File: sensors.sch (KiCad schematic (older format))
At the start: 8 parts, among them U12 LIS2HH12, U8 VL53L0X

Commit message: screen attached!
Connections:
- net RF_SD: no longer names the net of R58.2, U8.5 (XSHUT)
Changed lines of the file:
@@
 $Descr A4 11693 8268
 encoding utf-8
-Sheet 12 15
+Sheet 12 14
 Title ""
 Date ""
@@
 NoConn ~ 5900 3900
 $Comp
-L GND-RESCUE-DFTBoard #PWR0160
+L GND-RESCUE-DFTBoard #PWR0153
 U 1 1 58598433
 P 4550 4150
-F 0 "#PWR0160" H 4550 4150 30  0001 C CNN
+F 0 "#PWR0153" H 4550 4150 30  0001 C CNN
 F 1 "GND" H 4550 4080 30  0001 C CNN
 F 2 "" H 4550 4150 60  0001 C CNN
@@
 	4550 3400 4550 3300
 Connection ~ 4550 3300
-Text GLabel 6400 3300 2    60   Input ~ 0
-RF_SD
 $Comp
 L R R58
@@
 	1    0    0    -1
 $EndComp
-Wire Wire Line
-	5900 3300 6400 3300
-$Comp
-L +1.8V #PWR0161
+$Comp
+L +1.8V #PWR0154
 U 1 1 585987BD
 P 6200 2550
-F 0 "#PWR0161" H 6200 2690 20  0001 C CNN
+F 0 "#PWR0154" H 6200 2690 20  0001 C CNN
 F 1 "+1.8V" H 6200 2660 30  0000 C CNN
 F 2 "" H 6200 2550 60  0001 C CNN
@@
 Wire Wire Line
 	6300 3400 6300 2900
-Connection ~ 6100 3300
 Connection ~ 6300 3400
 Text GLabel 6400 3400 2    60   Input ~ 0
 RF_IRQ
 $Comp
-L +3.3V #PWR0162
+L +3.3V #PWR0155
 U 1 1 587438B2
 P 4000 3200
-F 0 "#PWR0162" H 4000 3050 50  0001 C CNN
+F 0 "#PWR0155" H 4000 3050 50  0001 C CNN
 F 1 "+3.3V" H 4000 3340 50  0000 C CNN
 F 2 "" H 4000 3200 50  0000 C CNN
@@
 $EndComp
 $Comp
-L GND-RESCUE-DFTBoard #PWR0163
+L GND-RESCUE-DFTBoard #PWR0156
 U 1 1 5983B53E
 P 6050 5400
-F 0 "#PWR0163" H 6050 5400 30  0001 C CNN
+F 0 "#PWR0156" H 6050 5400 30  0001 C CNN
 F 1 "GND" H 6050 5330 30  0001 C CNN
 F 2 "" H 6050 5400 60  0001 C CNN
@@
 I2C_SCLK
 $Comp
-L +1.8V #PWR0164
+L +1.8V #PWR0157
 U 1 1 5983B702
 P 4050 4500
-F 0 "#PWR0164" H 4050 4640 20  0001 C CNN
+F 0 "#PWR0157" H 4050 4640 20  0001 C CNN
 F 1 "+1.8V" H 4050 4610 30  0000 C CNN
 F 2 "" H 4050 4500 60  0001 C CNN
@@
 Connection ~ 4050 4750
 $Comp
-L +1.8V #PWR0165
+L +1.8V #PWR0158
 U 1 1 5983B8A0
 P 6150 4500
-F 0 "#PWR0165" H 6150 4640 20  0001 C CNN
+F 0 "#PWR0158" H 6150 4640 20  0001 C CNN
 F 1 "+1.8V" H 6150 4610 30  0000 C CNN
 F 2 "" H 6150 4500 60  0001 C CNN
@@
 	6450 4950 6450 4850
 $Comp
-L GND-RESCUE-DFTBoard #PWR0166
+L GND-RESCUE-DFTBoard #PWR0159
 U 1 1 5983BAD9
 P 6150 4950
-F 0 "#PWR0166" H 6150 4950 30  0001 C CNN
+F 0 "#PWR0159" H 6150 4950 30  0001 C CNN
 F 1 "GND" H 6150 4880 30  0001 C CNN
 F 2 "" H 6150 4950 60  0001 C CNN
@@
 $EndComp
 $Comp
-L GND-RESCUE-DFTBoard #PWR0167
+L GND-RESCUE-DFTBoard #PWR0160
 U 1 1 5983BAFC
 P 6450 4950
-F 0 "#PWR0167" H 6450 4950 30  0001 C CNN
+F 0 "#PWR0160" H 6450 4950 30  0001 C CNN
 F 1 "GND" H 6450 4880 30  0001 C CNN
 F 2 "" H 6450 4950 60  0001 C CNN
@@
 	6150 4500 6150 4650
 $Comp
-L GND-RESCUE-DFTBoard #PWR0168
+L GND-RESCUE-DFTBoard #PWR0161
 U 1 1 5983BD80
 P 4450 5350
-F 0 "#PWR0168" H 4450 5350 30  0001 C CNN
+F 0 "#PWR0161" H 4450 5350 30  0001 C CNN
 F 1 "GND" H 4450 5280 30  0001 C CNN
 F 2 "" H 4450 5350 60  0001 C CNN
@@
 NoConn ~ 4750 5150
 NoConn ~ 4750 5250
+Wire Wire Line
+	6100 3300 5900 3300
 $EndSCHEMATC

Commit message: using BOMs AWAY to create BOM
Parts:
- C110, C97: MFR (none) -> Murata; MPN (none) -> GRM188R71C104KA01D
- C111, C98: MFR (none) -> Murata; MPN (none) -> GRM21BR61A475KA73L
- R58, R59: MFR (none) -> Vishay Dale; MPN (none) -> CRCW040210K0FKED
- U8: MFR (none) -> STMicroelectronics; MPN (none) -> VL53L0CXV0DH/1

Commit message: just added NOTE field to BOMS AWAY
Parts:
- C110, C97: SPN (none) -> 490-1532-1-ND; SPR (none) -> Digikey
- C111, C98: SPN (none) -> 490-9750-1-ND; SPR (none) -> Digikey
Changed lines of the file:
@@
 F 4 "Murata" H 0 0 50 0001 C CNN "MFR"
 F 5 "GRM21BR61A475KA73L" H 0 0 50 0001 C CNN "MPN"
-F 6 "" H 0 0 50 0001 C CNN "SPR"
-F 7 "" H 0 0 50 0001 C CNN "SPN"
+F 6 "Digikey" H 0 0 50 0001 C CNN "SPR"
+F 7 "490-9750-1-ND" H 0 0 50 0001 C CNN "SPN"
 F 8 "" H 0 0 50 0001 C CNN "SPURL"
 	1    4000 3400
@@
 F 4 "Murata" H 0 0 50 0001 C CNN "MFR"
 F 5 "GRM188R71C104KA01D" H 0 0 50 0001 C CNN "MPN"
-F 6 "" H 0 0 50 0001 C CNN "SPR"
-F 7 "" H 0 0 50 0001 C CNN "SPN"
+F 6 "Digikey" H 0 0 50 0001 C CNN "SPR"
+F 7 "490-1532-1-ND" H 0 0 50 0001 C CNN "SPN"
 F 8 "" H 0 0 50 0001 C CNN "SPURL"
 	1    3700 3400
@@
 F 4 "Murata" H 0 0 50 0001 C CNN "MFR"
 F 5 "GRM21BR61A475KA73L" H 0 0 50 0001 C CNN "MPN"
-F 6 "" H 0 0 50 0001 C CNN "SPR"
-F 7 "" H 0 0 50 0001 C CNN "SPN"
+F 6 "Digikey" H 0 0 50 0001 C CNN "SPR"
+F 7 "490-9750-1-ND" H 0 0 50 0001 C CNN "SPN"
 F 8 "" H 0 0 50 0001 C CNN "SPURL"
 	1    6450 4750
@@
 F 4 "Murata" H 0 0 50 0001 C CNN "MFR"
 F 5 "GRM188R71C104KA01D" H 0 0 50 0001 C CNN "MPN"
-F 6 "" H 0 0 50 0001 C CNN "SPR"
-F 7 "" H 0 0 50 0001 C CNN "SPN"
+F 6 "Digikey" H 0 0 50 0001 C CNN "SPR"
+F 7 "490-1532-1-ND" H 0 0 50 0001 C CNN "SPN"
 F 8 "" H 0 0 50 0001 C CNN "SPURL"
 	1    6150 4750

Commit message: Complete BOM. all resistors now 0402
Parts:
- R58, R59: MFR Vishay Dale -> Yageo; MPN CRCW040210K0FKED -> RC0402FR-0710KL; SPN (none) -> 311-10.0KLRTR-ND; SPR (none) -> Digikey
- U12: MFR (none) -> STMicroelectronics; MPN (none) -> LIS2HH12TR; SPN (none) -> 497-15069-1-ND; SPR (none) -> Digikey
- U8: SPN (none) -> 497-16538-1-ND; SPR (none) -> Digikey

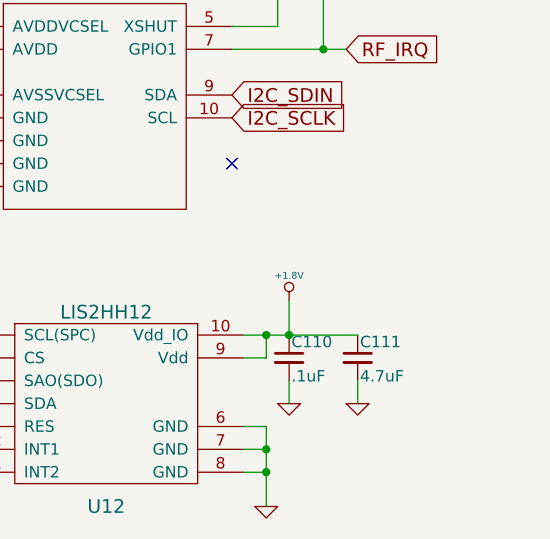
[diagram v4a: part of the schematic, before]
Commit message: added caps to audio
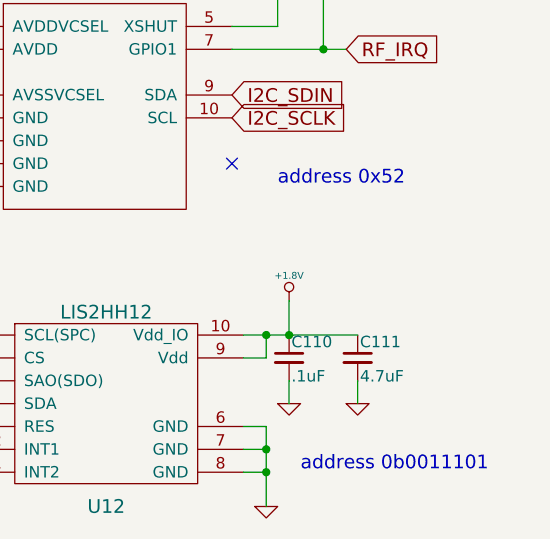
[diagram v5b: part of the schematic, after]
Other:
- note added: "address 0b0011101"
- note added: "address 0x52"
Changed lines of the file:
@@
 $Descr A4 11693 8268
 encoding utf-8
-Sheet 12 14
+Sheet 11 14
 Title ""
 Date ""
@@
 $EndComp
 $Comp
-L GND-RESCUE-DFTBoard #PWR0153
+L GND-RESCUE-DFTBoard #PWR0154
 U 1 1 58598433
 P 4550 4150
-F 0 "#PWR0153" H 4550 4150 30  0001 C CNN
+F 0 "#PWR0154" H 4550 4150 30  0001 C CNN
 F 1 "GND" H 4550 4080 30  0001 C CNN
 F 2 "" H 4550 4150 60  0001 C CNN
@@
 $EndComp
 $Comp
-L +1.8V #PWR0154
+L +1.8V #PWR0155
 U 1 1 585987BD
 P 6200 2550
-F 0 "#PWR0154" H 6200 2690 20  0001 C CNN
+F 0 "#PWR0155" H 6200 2690 20  0001 C CNN
 F 1 "+1.8V" H 6200 2660 30  0000 C CNN
 F 2 "" H 6200 2550 60  0001 C CNN
@@
 $EndComp
 $Comp
-L +3.3V #PWR0155
+L +3.3V #PWR0156
 U 1 1 587438B2
 P 4000 3200
-F 0 "#PWR0155" H 4000 3050 50  0001 C CNN
+F 0 "#PWR0156" H 4000 3050 50  0001 C CNN
 F 1 "+3.3V" H 4000 3340 50  0000 C CNN
 F 2 "" H 4000 3200 50  0000 C CNN
@@
 $EndComp
 $Comp
-L GND-RESCUE-DFTBoard #PWR0156
+L GND-RESCUE-DFTBoard #PWR0157
 U 1 1 5983B53E
 P 6050 5400
-F 0 "#PWR0156" H 6050 5400 30  0001 C CNN
+F 0 "#PWR0157" H 6050 5400 30  0001 C CNN
 F 1 "GND" H 6050 5330 30  0001 C CNN
 F 2 "" H 6050 5400 60  0001 C CNN
@@
 $EndComp
 $Comp
-L +1.8V #PWR0157
+L +1.8V #PWR0158
 U 1 1 5983B702
 P 4050 4500
-F 0 "#PWR0157" H 4050 4640 20  0001 C CNN
+F 0 "#PWR0158" H 4050 4640 20  0001 C CNN
 F 1 "+1.8V" H 4050 4610 30  0000 C CNN
 F 2 "" H 4050 4500 60  0001 C CNN
@@
 $EndComp
 $Comp
-L +1.8V #PWR0158
+L +1.8V #PWR0159
 U 1 1 5983B8A0
 P 6150 4500
-F 0 "#PWR0158" H 6150 4640 20  0001 C CNN
+F 0 "#PWR0159" H 6150 4640 20  0001 C CNN
 F 1 "+1.8V" H 6150 4610 30  0000 C CNN
 F 2 "" H 6150 4500 60  0001 C CNN
@@
 $EndComp
 $Comp
-L GND-RESCUE-DFTBoard #PWR0159
+L GND-RESCUE-DFTBoard #PWR0160
 U 1 1 5983BAD9
 P 6150 4950
-F 0 "#PWR0159" H 6150 4950 30  0001 C CNN
+F 0 "#PWR0160" H 6150 4950 30  0001 C CNN
 F 1 "GND" H 6150 4880 30  0001 C CNN
 F 2 "" H 6150 4950 60  0001 C CNN
@@
 $EndComp
 $Comp
-L GND-RESCUE-DFTBoard #PWR0160
+L GND-RESCUE-DFTBoard #PWR0161
 U 1 1 5983BAFC
 P 6450 4950
-F 0 "#PWR0160" H 6450 4950 30  0001 C CNN
+F 0 "#PWR0161" H 6450 4950 30  0001 C CNN
 F 1 "GND" H 6450 4880 30  0001 C CNN
 F 2 "" H 6450 4950 60  0001 C CNN
@@
 $EndComp
 $Comp
-L GND-RESCUE-DFTBoard #PWR0161
+L GND-RESCUE-DFTBoard #PWR0162
 U 1 1 5983BD80
 P 4450 5350
-F 0 "#PWR0161" H 4450 5350 30  0001 C CNN
+F 0 "#PWR0162" H 4450 5350 30  0001 C CNN
 F 1 "GND" H 4450 5280 30  0001 C CNN
 F 2 "" H 4450 5350 60  0001 C CNN
@@
 NoConn ~ 4750 5150
 NoConn ~ 4750 5250
+Text Notes 6100 4000 0    60   ~ 0
+address 0x52
+Text Notes 6200 5250 0    60   ~ 0
+address 0b0011101
 $EndSCHEMATC

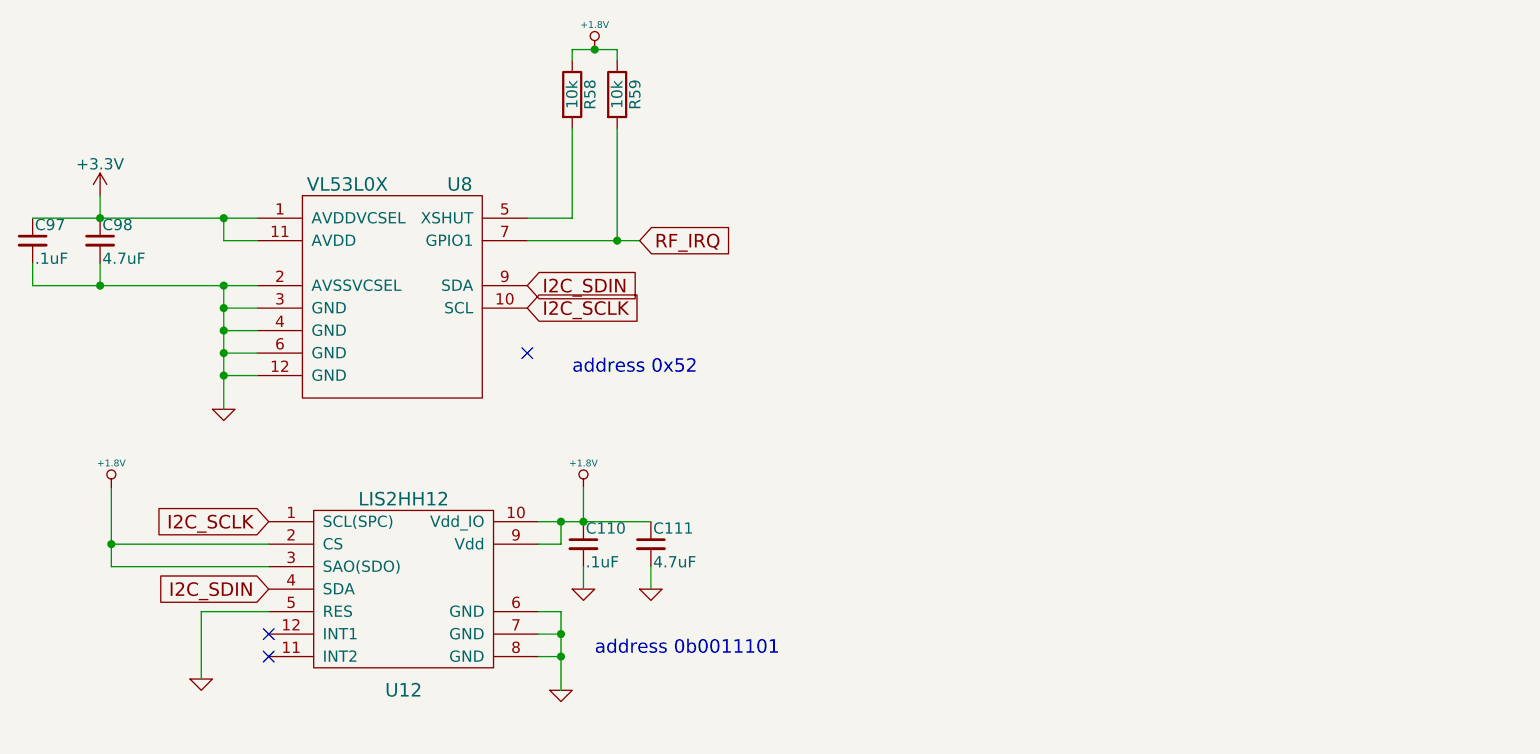
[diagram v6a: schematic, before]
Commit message: about to resize all silkscreen text to 0.5
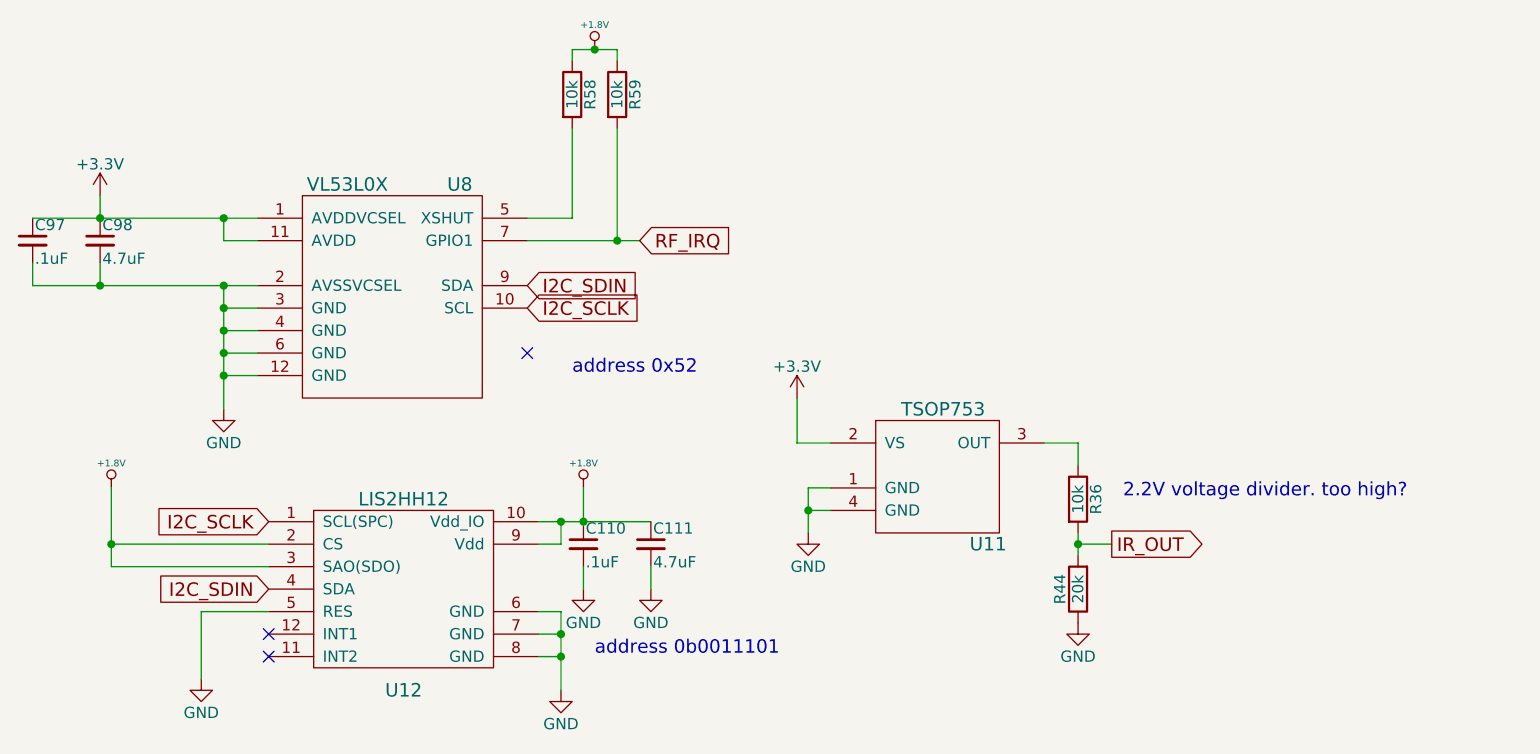
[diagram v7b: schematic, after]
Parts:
- added R36: 10k, Resistors_SMD:R_0402, symbol R
- added R44: 20k, Resistors_SMD:R_0402, symbol R
- added U11: TSOP753, DFTcustom:TSOP753_755, symbol TSOP753
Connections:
- net +3V3: now also U11.2 (VS)
- net GND: now also R44.1, U11.1 (GND), U11.4 (GND)
- new net: R36.1, U11.3 (OUT)
- new net IR_OUT: R36.2, R44.2
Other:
- note added: "2.2V voltage divider. too high?"
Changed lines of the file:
@@
 LIBS:er-con06hb-1
 LIBS:jack_trs_4pins
+LIBS:NorBot
+LIBS:CC2500
 EELAYER 25 0
 EELAYER END
 $Descr A4 11693 8268
 encoding utf-8
-Sheet 11 14
+Sheet 11 15
 Title ""
 Date ""
@@
 $EndComp
 $Comp
-L GND-RESCUE-DFTBoard #PWR0154
-U 1 1 58598433
-P 4550 4150
-F 0 "#PWR0154" H 4550 4150 30  0001 C CNN
-F 1 "GND" H 4550 4080 30  0001 C CNN
-F 2 "" H 4550 4150 60  0001 C CNN
-F 3 "" H 4550 4150 60  0001 C CNN
-	1    4550 4150
-	1    0    0    -1
-$EndComp
-$Comp
 L C_Small C98
 U 1 1 585984E0
@@
 $EndComp
 $Comp
-L +1.8V #PWR0155
+L +1.8V #PWR0149
 U 1 1 585987BD
 P 6200 2550
-F 0 "#PWR0155" H 6200 2690 20  0001 C CNN
+F 0 "#PWR0149" H 6200 2690 20  0001 C CNN
 F 1 "+1.8V" H 6200 2660 30  0000 C CNN
 F 2 "" H 6200 2550 60  0001 C CNN
@@
 $EndComp
 $Comp
-L +3.3V #PWR0156
+L +3.3V #PWR0150
 U 1 1 587438B2
 P 4000 3200
-F 0 "#PWR0156" H 4000 3050 50  0001 C CNN
+F 0 "#PWR0150" H 4000 3050 50  0001 C CNN
 F 1 "+3.3V" H 4000 3340 50  0000 C CNN
 F 2 "" H 4000 3200 50  0000 C CNN
@@
 $EndComp
 $Comp
-L GND-RESCUE-DFTBoard #PWR0157
-U 1 1 5983B53E
-P 6050 5400
-F 0 "#PWR0157" H 6050 5400 30  0001 C CNN
-F 1 "GND" H 6050 5330 30  0001 C CNN
-F 2 "" H 6050 5400 60  0001 C CNN
-F 3 "" H 6050 5400 60  0001 C CNN
-	1    6050 5400
-	1    0    0    -1
-$EndComp
-$Comp
-L +1.8V #PWR0158
+L +1.8V #PWR0151
 U 1 1 5983B702
 P 4050 4500
-F 0 "#PWR0158" H 4050 4640 20  0001 C CNN
+F 0 "#PWR0151" H 4050 4640 20  0001 C CNN
 F 1 "+1.8V" H 4050 4610 30  0000 C CNN
 F 2 "" H 4050 4500 60  0001 C CNN
@@
 $EndComp
 $Comp
-L +1.8V #PWR0159
+L +1.8V #PWR0152
 U 1 1 5983B8A0
 P 6150 4500
-F 0 "#PWR0159" H 6150 4640 20  0001 C CNN
+F 0 "#PWR0152" H 6150 4640 20  0001 C CNN
 F 1 "+1.8V" H 6150 4610 30  0000 C CNN
 F 2 "" H 6150 4500 60  0001 C CNN
@@
 F 8 "" H 0   0   50  0001 C CNN "SPURL"
 	1    6150 4750
-	1    0    0    -1
-$EndComp
-$Comp
-L GND-RESCUE-DFTBoard #PWR0160
-U 1 1 5983BAD9
-P 6150 4950
-F 0 "#PWR0160" H 6150 4950 30  0001 C CNN
-F 1 "GND" H 6150 4880 30  0001 C CNN
-F 2 "" H 6150 4950 60  0001 C CNN
-F 3 "" H 6150 4950 60  0001 C CNN
-	1    6150 4950
-	1    0    0    -1
-$EndComp
-$Comp
-L GND-RESCUE-DFTBoard #PWR0161
-U 1 1 5983BAFC
-P 6450 4950
-F 0 "#PWR0161" H 6450 4950 30  0001 C CNN
-F 1 "GND" H 6450 4880 30  0001 C CNN
-F 2 "" H 6450 4950 60  0001 C CNN
-F 3 "" H 6450 4950 60  0001 C CNN
-	1    6450 4950
-	1    0    0    -1
-$EndComp
-$Comp
-L GND-RESCUE-DFTBoard #PWR0162
-U 1 1 5983BD80
-P 4450 5350
-F 0 "#PWR0162" H 4450 5350 30  0001 C CNN
-F 1 "GND" H 4450 5280 30  0001 C CNN
-F 2 "" H 4450 5350 60  0001 C CNN
-F 3 "" H 4450 5350 60  0001 C CNN
-	1    4450 5350
 	1    0    0    -1
 $EndComp
@@
 address 0b0011101
 NoConn ~ 5900 3900
+$Comp
+L GND #PWR0153
+U 1 1 5A3317E1
+P 6150 4950
+F 0 "#PWR0153" H 6150 4700 50  0001 C CNN
+F 1 "GND" H 6150 4800 50  0000 C CNN
+F 2 "" H 6150 4950 50  0001 C CNN
+F 3 "" H 6150 4950 50  0001 C CNN
+	1    6150 4950
+	1    0    0    -1
+$EndComp
+$Comp
+L GND #PWR0154
+U 1 1 5A33180B
+P 6450 4950
+F 0 "#PWR0154" H 6450 4700 50  0001 C CNN
+F 1 "GND" H 6450 4800 50  0000 C CNN
+F 2 "" H 6450 4950 50  0001 C CNN
+F 3 "" H 6450 4950 50  0001 C CNN
+	1    6450 4950
+	1    0    0    -1
+$EndComp
+$Comp
+L GND #PWR0155
+U 1 1 5A33182E
+P 6050 5400
+F 0 "#PWR0155" H 6050 5150 50  0001 C CNN
+F 1 "GND" H 6050 5250 50  0000 C CNN
+F 2 "" H 6050 5400 50  0001 C CNN
+F 3 "" H 6050 5400 50  0001 C CNN
+	1    6050 5400
+	1    0    0    -1
+$EndComp
+$Comp
+L GND #PWR0156
+U 1 1 5A331851
+P 4450 5350
+F 0 "#PWR0156" H 4450 5100 50  0001 C CNN
+F 1 "GND" H 4450 5200 50  0000 C CNN
+F 2 "" H 4450 5350 50  0001 C CNN
+F 3 "" H 4450 5350 50  0001 C CNN
+	1    4450 5350
+	1    0    0    -1
+$EndComp
+$Comp
+L GND #PWR0157
+U 1 1 5A331874
+P 4550 4150
+F 0 "#PWR0157" H 4550 3900 50  0001 C CNN
+F 1 "GND" H 4550 4000 50  0000 C CNN
+F 2 "" H 4550 4150 50  0001 C CNN
+F 3 "" H 4550 4150 50  0001 C CNN
+	1    4550 4150
+	1    0    0    -1
+$EndComp
+$Comp
+L TSOP753 U11
+U 1 1 5A339135
+P 7700 4400
+F 0 "U11" H 7950 4050 60  0000 C CNN
+F 1 "TSOP753" H 7750 4650 60  0000 C CNN
+F 2 "DFTcustom:TSOP753_755" H 7650 4550 60  0001 C CNN
+F 3 "" H 7650 4550 60  0001 C CNN
+	1    7700 4400
+	1    0    0    -1
+$EndComp
+$Comp
+L GND #PWR0158
+U 1 1 5A339225
+P 7150 4700
+F 0 "#PWR0158" H 7150 4450 50  0001 C CNN
+F 1 "GND" H 7150 4550 50  0000 C CNN
+F 2 "" H 7150 4700 50  0001 C CNN
+F 3 "" H 7150 4700 50  0001 C CNN
+	1    7150 4700
+	1    0    0    -1
+$EndComp
+Wire Wire Line
+	7250 4500 7150 4500
+Wire Wire Line
+	7150 4500 7150 4700
+Wire Wire Line
+	7250 4600 7150 4600
+Connection ~ 7150 4600
+Wire Wire Line
+	7250 4300 7100 4300
+Wire Wire Line
+	7100 4300 7100 4100
+$Comp
+L R R36
+U 1 1 5A33AB4F
+P 8350 4550
+F 0 "R36" V 8430 4550 50  0000 C CNN
+F 1 "10k" V 8350 4550 50  0000 C CNN
+F 2 "Resistors_SMD:R_0402" V 8280 4550 50  0001 C CNN
+F 3 "" H 8350 4550 50  0001 C CNN
+F 4 "Yageo" H 3450 -1100 50  0001 C CNN "MFR"
+F 5 "RC0402FR-0710KL" H 3450 -1100 50  0001 C CNN "MPN"
+F 6 "Digikey" H 3450 -1100 50  0001 C CNN "SPR"
+F 7 "311-10.0KLRTR-ND" H 3450 -1100 50  0001 C CNN "SPN"
+F 8 "" H 3450 -1100 50  0001 C CNN "SPURL"
+	1    8350 4550
+	1    0    0    -1
+$EndComp
+Wire Wire Line
+	8200 4300 8350 4300
+Wire Wire Line
+	8350 4300 8350 4400
+$Comp
+L R R44
+U 1 1 5A33ACEC
+P 8350 4950
+F 0 "R44" V 8430 4950 50  0000 C CNN
+F 1 "20k" V 8350 4950 50  0000 C CNN
+F 2 "Resistors_SMD:R_0402" V 8280 4950 50  0001 C CNN
+F 3 "" H 8350 4950 50  0001 C CNN
+F 4 "Yageo" H -850 3050 50  0001 C CNN "MFR"
+F 5 "RC0402FR-0720KL" H -850 3050 50  0001 C CNN "MPN"
+F 6 "Digikey" H -850 3050 50  0001 C CNN "SPR"
+F 7 "311-20.0KLRCT-ND" H -850 3050 50  0001 C CNN "SPN"
+F 8 "" H -850 3050 50  0001 C CNN "SPURL"
+	1    8350 4950
+	-1   0    0    1
+$EndComp
+Wire Wire Line
+	8350 4700 8350 4800
+$Comp
+L GND #PWR0159
+U 1 1 5A33AD51
+P 8350 5100
+F 0 "#PWR0159" H 8350 4850 50  0001 C CNN
+F 1 "GND" H 8350 4950 50  0000 C CNN
+F 2 "" H 8350 5100 50  0001 C CNN
+F 3 "" H 8350 5100 50  0001 C CNN
+	1    8350 5100
+	1    0    0    -1
+$EndComp
+Text GLabel 8500 4750 2    60   Output ~ 0
+IR_OUT
+Wire Wire Line
+	8500 4750 8350 4750
+Connection ~ 8350 4750
+Text Notes 8550 4550 0    60   ~ 0
+2.2V voltage divider. too high?
+$Comp
+L +3.3V #PWR0160
+U 1 1 5A346128
+P 7100 4100
+F 0 "#PWR0160" H 7100 3950 50  0001 C CNN
+F 1 "+3.3V" H 7100 4240 50  0000 C CNN
+F 2 "" H 7100 4100 50  0000 C CNN
+F 3 "" H 7100 4100 50  0000 C CNN
+	1    7100 4100
+	1    0    0    -1
+$EndComp
 $EndSCHEMATC
